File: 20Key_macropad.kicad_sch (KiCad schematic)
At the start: 86 parts, among them J1 USB4085-GF-A_REVB, J2 Conn_01x15_Pin, J3 Conn_01x15_Socket, SW1 SW_Push, SW10 SW_Push, SW11 SW_Push, SW12 SW_Push, SW13 SW_Push, SW14 SW_Push, SW15 SW_Push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

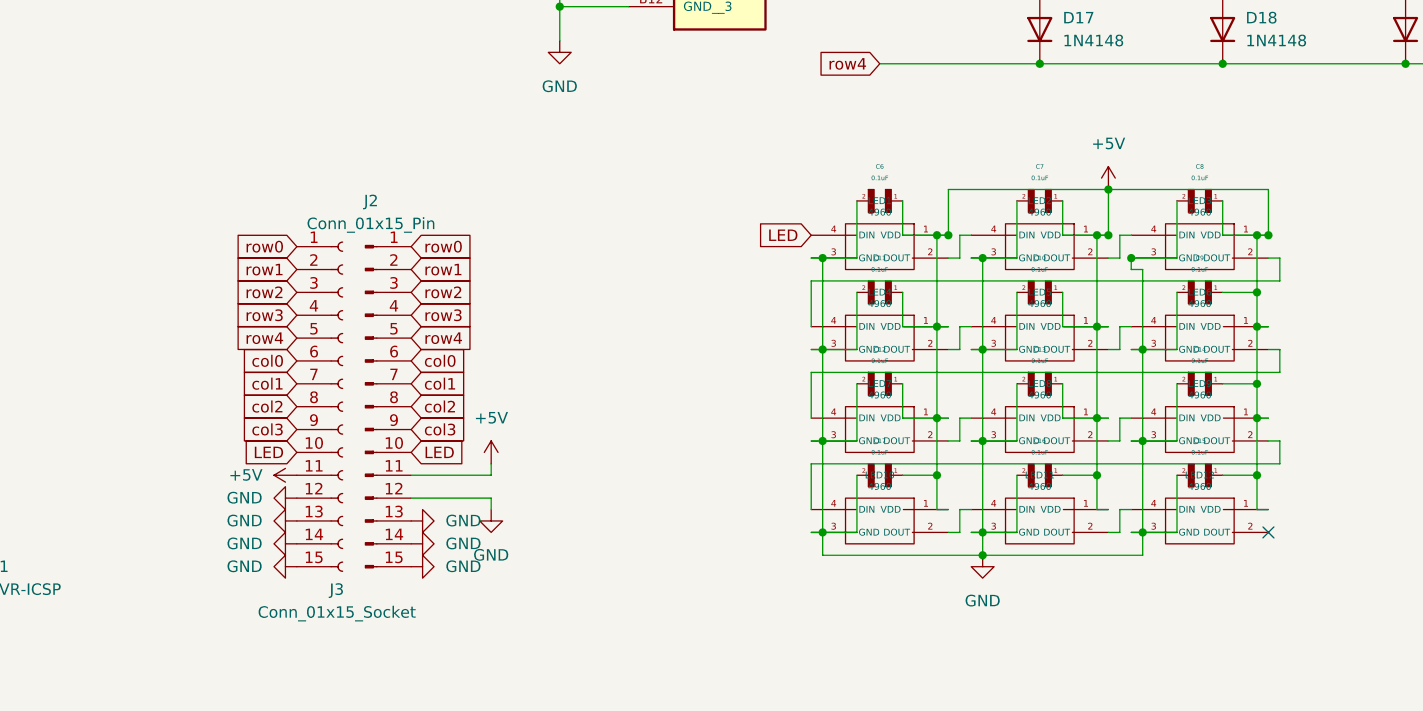
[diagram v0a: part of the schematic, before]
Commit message: fix issue with LEDs
LED's were facing the wrong way due to an issue withe the footprint. also removed the capacitors as they were not needed with only 12 lights
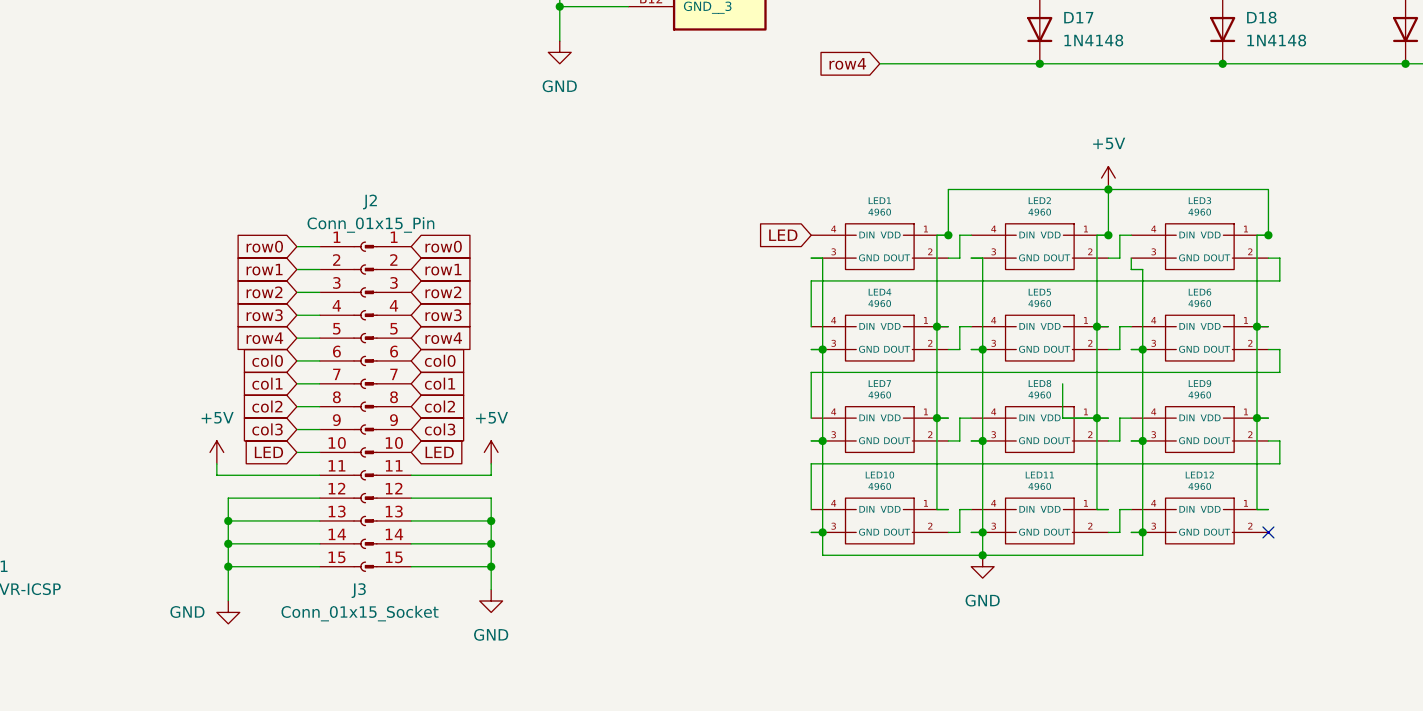
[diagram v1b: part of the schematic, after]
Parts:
- removed C10, C11, C12, C13, C14, C15, C16, C17, C6, C7, C8, C9: 0.1uF, Snapeda:CL21B103KBANNNC_CAPC2012X140N, symbol Snapeda_kicad_sym:CL21B103KBANNNC
- R5: footprint Resistor_THT:R_Axial_DIN0207_L6.3mm_D2.5mm_P7.62mm_Horizontal -> Resistor_THT:R_Axial_DIN0204_L3.6mm_D1.6mm_P5.08mm_Horizontal
- SW1, SW10, SW11, SW12, SW13, SW14, SW15, SW16, SW17, SW18, SW19, SW2, SW20, SW3, SW4, SW5, SW6, SW7, SW8, SW9: footprint Button_Switch_Keyboard:SW_Cherry_MX_1.00u_PCB -> Snapeda:SW_Cherry_MX_1.00u_PCB
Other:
- moved on the sheet: J3
